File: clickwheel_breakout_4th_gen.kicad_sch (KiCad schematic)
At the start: 7 parts

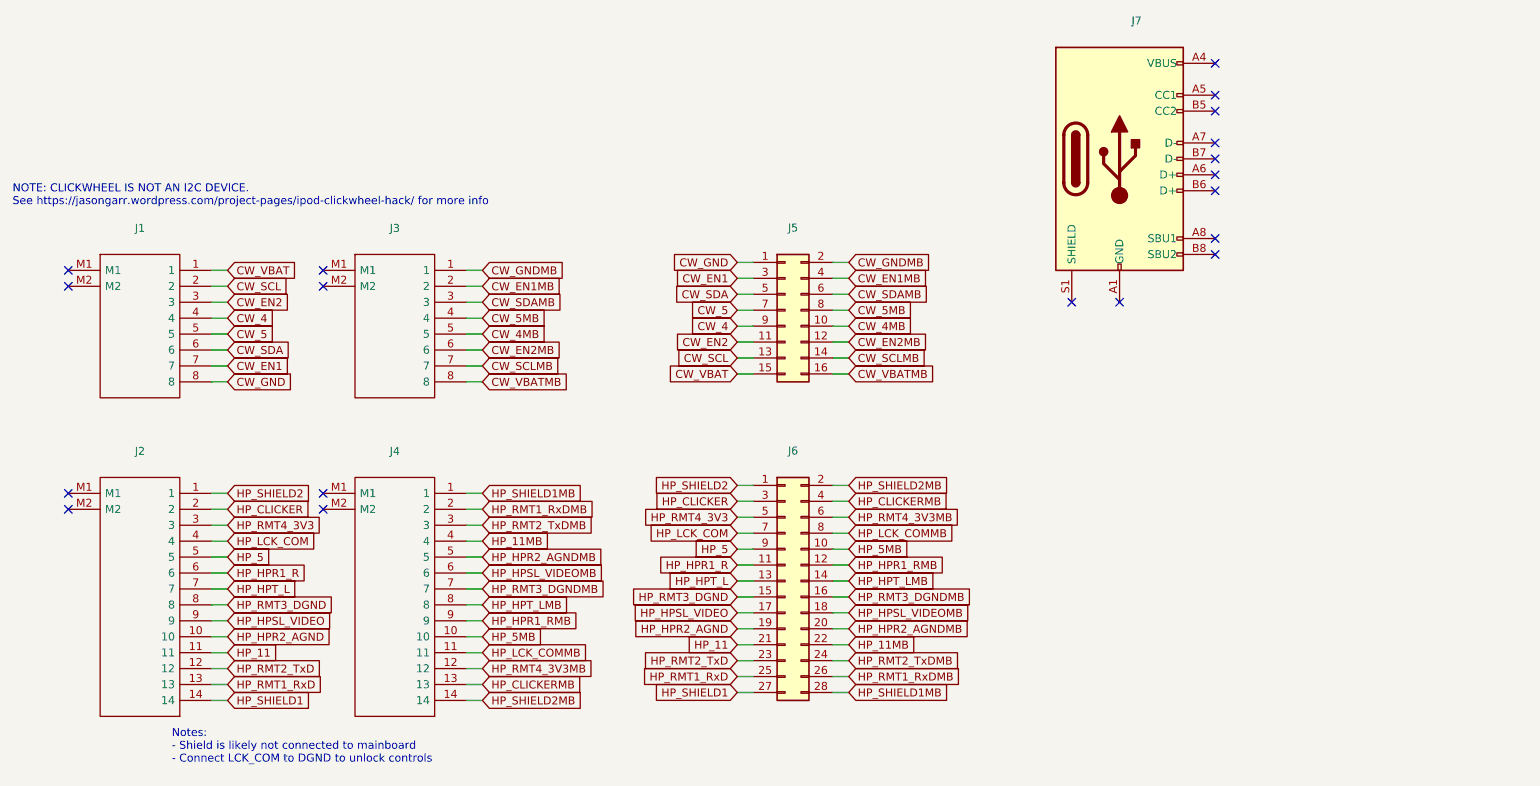
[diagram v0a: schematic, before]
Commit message: kibot: add initial generated QR code
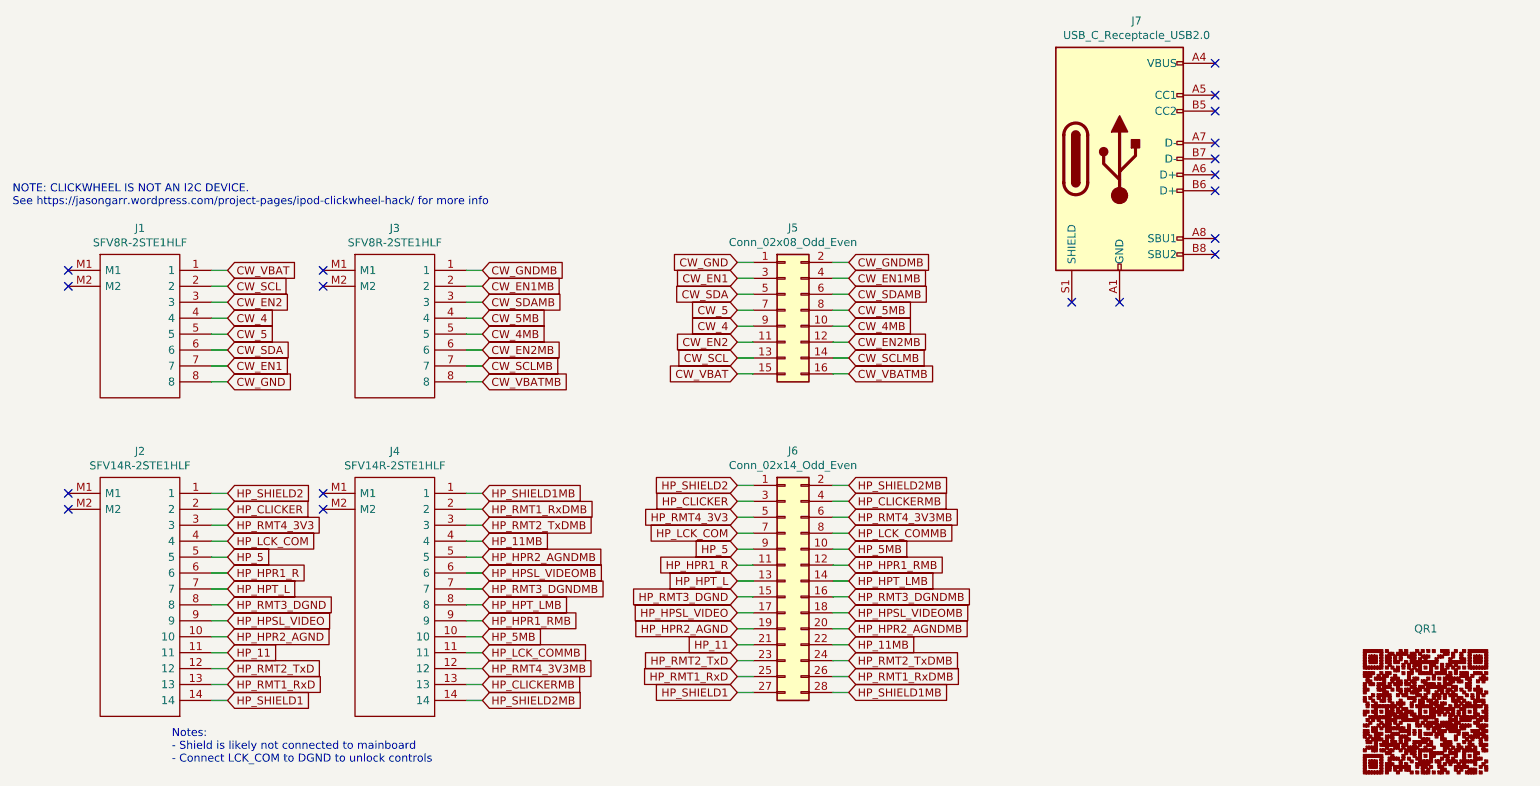
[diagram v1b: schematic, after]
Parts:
- added QR1: (no value), QR:QR_data, symbol clickwheel_breakout_4th_gen-qr:QR_data
- J1, J3: value (none) -> SFV8R-2STE1HLF; footprint (none) -> Gigahawk:SFV8R2STE1HLF
- J2, J4: value (none) -> SFV14R-2STE1HLF; footprint (none) -> Gigahawk:SFV14R2STE1HLF
- J5: value (none) -> Conn_02x08_Odd_Even; footprint (none) -> Connector_PinHeader_2.54mm:PinHeader_2x08_P2.54mm_Vertical
- J6: value (none) -> Conn_02x14_Odd_Even; footprint (none) -> Connector_PinHeader_2.54mm:PinHeader_2x14_P2.54mm_Vertical
- J7: value (none) -> USB_C_Receptacle_USB2.0; footprint (none) -> Gigahawk:USB_C_Receptacle_GCT_USB4085
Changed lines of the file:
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@@
     (in_bom yes) (on_board yes)
     (property "Reference" "J2" (id 0) (at 49.53 106.299 0))
-    (property "Value" "" (id 1) (at 49.53 108.6104 0))
-    (property "Footprint" "" (id 2) (at 57.15 110.49 0)
+    (property "Value" "SFV14R-2STE1HLF" (id 1) (at 49.53 108.6104 0))
+    (property "Footprint" "Gigahawk:SFV14R2STE1HLF" (id 2) (at 57.15 110.49 0)
       (effects (font (size 1.27 1.27)) (justify left) hide)
     )
@@
     (in_bom yes) (on_board yes)
     (property "Reference" "J1" (id 0) (at 49.53 70.739 0))
-    (property "Value" "" (id 1) (at 49.53 73.0504 0))
-    (property "Footprint" "" (id 2) (at 57.15 74.93 0)
+    (property "Value" "SFV8R-2STE1HLF" (id 1) (at 49.53 73.0504 0))
+    (property "Footprint" "Gigahawk:SFV8R2STE1HLF" (id 2) (at 57.15 74.93 0)
       (effects (font (size 1.27 1.27)) (justify left) hide)
     )
@@
     (in_bom yes) (on_board yes)
     (property "Reference" "J4" (id 0) (at 90.17 106.299 0))
-    (property "Value" "" (id 1) (at 90.17 108.6104 0))
-    (property "Footprint" "" (id 2) (at 97.79 110.49 0)
+    (property "Value" "SFV14R-2STE1HLF" (id 1) (at 90.17 108.6104 0))
+    (property "Footprint" "Gigahawk:SFV14R2STE1HLF" (id 2) (at 97.79 110.49 0)
       (effects (font (size 1.27 1.27)) (justify left) hide)
     )
@@
     (in_bom yes) (on_board yes)
     (property "Reference" "J3" (id 0) (at 90.17 70.739 0))
-    (property "Value" "" (id 1) (at 90.17 73.0504 0))
-    (property "Footprint" "" (id 2) (at 97.79 74.93 0)
+    (property "Value" "SFV8R-2STE1HLF" (id 1) (at 90.17 73.0504 0))
+    (property "Footprint" "Gigahawk:SFV8R2STE1HLF" (id 2) (at 97.79 74.93 0)
       (effects (font (size 1.27 1.27)) (justify left) hide)
     )
@@
     (in_bom yes) (on_board yes)
     (property "Reference" "J5" (id 0) (at 153.67 70.6882 0))
-    (property "Value" "" (id 1) (at 153.67 72.9996 0))
-    (property "Footprint" "" (id 2) (at 152.4 83.82 0)
+    (property "Value" "Conn_02x08_Odd_Even" (id 1) (at 153.67 72.9996 0))
+    (property "Footprint" "Connector_PinHeader_2.54mm:PinHeader_2x08_P2.54mm_Vertical" (id 2) (at 152.4 83.82 0)
       (effects (font (size 1.27 1.27)) hide)
     )
@@
     (in_bom yes) (on_board yes)
     (property "Reference" "J6" (id 0) (at 153.67 106.2482 0))
-    (property "Value" "" (id 1) (at 153.67 108.5596 0))
-    (property "Footprint" "" (id 2) (at 152.4 127 0)
+    (property "Value" "Conn_02x14_Odd_Even" (id 1) (at 153.67 108.5596 0))
+    (property "Footprint" "Connector_PinHeader_2.54mm:PinHeader_2x14_P2.54mm_Vertical" (id 2) (at 152.4 127 0)
       (effects (font (size 1.27 1.27)) hide)
     )
@@
     (in_bom yes) (on_board yes)
     (property "Reference" "J7" (id 0) (at 208.4578 37.6682 0))
-    (property "Value" "" (id 1) (at 208.4578 39.9796 0))
-    (property "Footprint" "" (id 2) (at 209.55 59.69 0)
+    (property "Value" "USB_C_Receptacle_USB2.0" (id 1) (at 208.4578 39.9796 0))
+    (property "Footprint" "Gigahawk:USB_C_Receptacle_GCT_USB4085" (id 2) (at 209.55 59.69 0)
       (effects (font (size 1.27 1.27)) hide)
     )
@@
     (pin "S1")
   )
+  (symbol (lib_id "clickwheel_breakout_4th_gen-qr:QR_data") (at 254.635 147.955 0) (unit 1)
+    (in_bom no) (on_board yes)
+    (property "Reference" "QR1" (id 0) (at 252.73 134.62 0)
+      (effects (font (size 1.27 1.27)) (justify left))
+    )
+    (property "Value" "" (id 1) (at 250.825 136.525 0)
+      (effects (font (size 1.27 1.27)) (justify left))
+    )
+    (property "Footprint" "QR:QR_data" (id 2) (at 254.635 158.405 0)
+      (effects (font (size 1.27 1.27)) hide)
+    )
+    (property "Datasheet" "" (id 3) (at 254.635 160.105 0)
+      (effects (font (size 1.27 1.27)) hide)
+    )
+    (property "qr_version" "7" (id 4) (at 254.635 161.805 0)
+      (effects (font (size 1.27 1.27)) hide)
+    )
+    (property "qr_size" "45" (id 5) (at 254.635 163.505 0)
+      (effects (font (size 1.27 1.27)) hide)
+    )
+    (property "qr_ecc" "0,1" (id 6) (at 254.635 165.205 0)
+      (effects (font (size 1.27 1.27)) hide)
+    )
+    (property "qr_mask" "3" (id 7) (at 254.635 166.905 0)
+      (effects (font (size 1.27 1.27)) hide)
+    )
+    (property "qr_text" "OOPSIE WOOPSIE!! Uwu We make a fucky wucky!! A wittle fucko boingo! The code monkeys at our headquarters are working VEWY HAWD to fix this!\n" (id 8) (at 254.635 168.605 0)
+      (effects (font (size 1.27 1.27)) hide)
+    )
+  )
   (sheet_instances
     (path "/" (page "1"))
@@
       (reference "J7") (unit 1) (value "USB_C_Receptacle_USB2.0") (footprint "Gigahawk:USB_C_Receptacle_GCT_USB4085")
     )
-  )
+    (path "/90211c05-3354-414f-a4b4-596a1a6ea313"
+      (reference "QR1") (unit 1) (value "QR_data") (footprint "QR:QR_data")
+    )
+  )

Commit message: ci: add CI (#1)
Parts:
- removed QR1: (no value), QR:QR_data, symbol clickwheel_breakout_4th_gen-qr:QR_data
- added QR1: (no value), symbol QR:QR_data
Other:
- title: (none) -> iPod 4th Gen Clickwheel Breakout
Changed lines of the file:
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@@
 (kicad_sch (version 20211123) (generator eeschema)
   (paper "A4")
+  (title_block
+    (title "iPod 4th Gen Clickwheel Breakout")
+    (date "${DATE}")
+    (rev "${REVISION}")
+  )
   (no_connect (at 78.74 77.47))
   (no_connect (at 78.74 80.01))
@@
     (pin "S1")
   )
-  (symbol (lib_id "clickwheel_breakout_4th_gen-qr:QR_data") (at 254.635 147.955 0) (unit 1)
-    (in_bom no) (on_board yes)
-    (property "Reference" "QR1" (id 0) (at 252.73 134.62 0)
-      (effects (font (size 1.27 1.27)) (justify left))
-    )
-    (property "Value" "" (id 1) (at 250.825 136.525 0)
-      (effects (font (size 1.27 1.27)) (justify left))
-    )
-    (property "Footprint" "QR:QR_data" (id 2) (at 254.635 158.405 0)
-      (effects (font (size 1.27 1.27)) hide)
-    )
-    (property "Datasheet" "" (id 3) (at 254.635 160.105 0)
-      (effects (font (size 1.27 1.27)) hide)
-    )
-    (property "qr_version" "7" (id 4) (at 254.635 161.805 0)
-      (effects (font (size 1.27 1.27)) hide)
-    )
-    (property "qr_size" "45" (id 5) (at 254.635 163.505 0)
-      (effects (font (size 1.27 1.27)) hide)
-    )
-    (property "qr_ecc" "0,1" (id 6) (at 254.635 165.205 0)
-      (effects (font (size 1.27 1.27)) hide)
-    )
-    (property "qr_mask" "3" (id 7) (at 254.635 166.905 0)
-      (effects (font (size 1.27 1.27)) hide)
-    )
-    (property "qr_text" "OOPSIE WOOPSIE!! Uwu We make a fucky wucky!! A wittle fucko boingo! The code monkeys at our headquarters are working VEWY HAWD to fix this!\n" (id 8) (at 254.635 168.605 0)
+  (symbol (lib_id "QR:QR_data") (at 260.985 145.415 0) (unit 1)
+    (in_bom no) (on_board yes) (fields_autoplaced)
+    (property "Reference" "QR1" (id 0) (at 260.885 130.81 0))
+    (property "Value" "" (id 1) (at 260.885 133.35 0))
+    (property "Footprint" "" (id 2) (at 260.985 158.365 0)
+      (effects (font (size 1.27 1.27)) hide)
+    )
+    (property "Datasheet" "" (id 3) (at 260.985 160.065 0)
+      (effects (font (size 1.27 1.27)) hide)
+    )
+    (property "qr_version" "7" (id 4) (at 260.985 161.765 0)
+      (effects (font (size 1.27 1.27)) hide)
+    )
+    (property "qr_size" "45" (id 5) (at 260.985 163.465 0)
+      (effects (font (size 1.27 1.27)) hide)
+    )
+    (property "qr_ecc" "0,1" (id 6) (at 260.985 165.165 0)
+      (effects (font (size 1.27 1.27)) hide)
+    )
+    (property "qr_mask" "3" (id 7) (at 260.985 166.865 0)
+      (effects (font (size 1.27 1.27)) hide)
+    )
+    (property "qr_text" "OOPSIE WOOPSIE!! Uwu We make a fucky wucky!! A wittle fucko boingo! The code monkeys at our headquarters are working VEWY HAWD to fix this!\n" (id 8) (at 260.985 168.565 0)
       (effects (font (size 1.27 1.27)) hide)
     )
@@
       (reference "J7") (unit 1) (value "USB_C_Receptacle_USB2.0") (footprint "Gigahawk:USB_C_Receptacle_GCT_USB4085")
     )
-    (path "/90211c05-3354-414f-a4b4-596a1a6ea313"
+    (path "/e1d122d3-e0b7-44f3-b2d8-4baa56b4ef17"
       (reference "QR1") (unit 1) (value "QR_data") (footprint "QR:QR_data")
     )

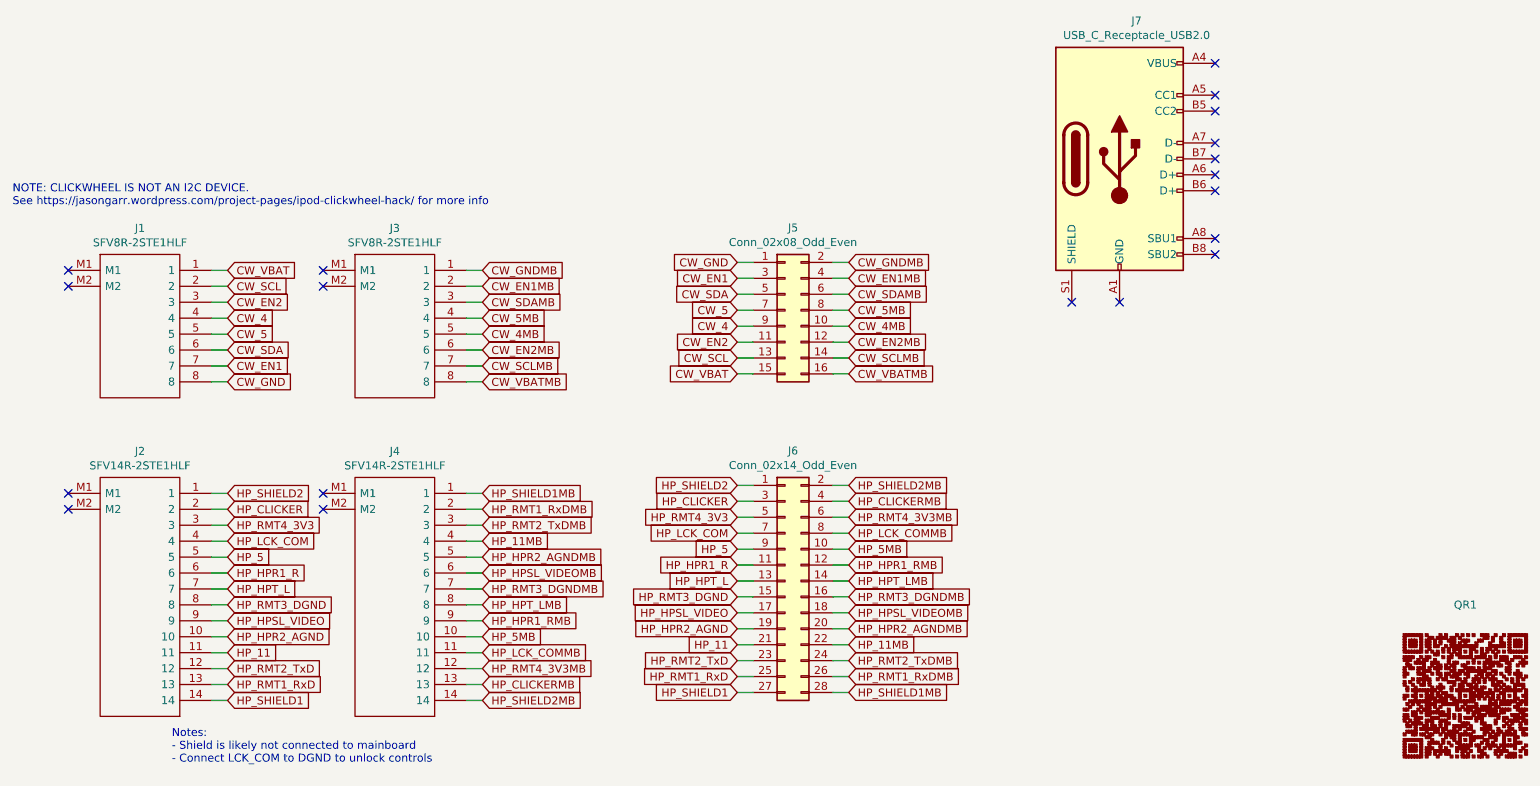
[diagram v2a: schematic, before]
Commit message: silkscreen: add label for missing headphone AGND
- silkscreen: add connection instructions
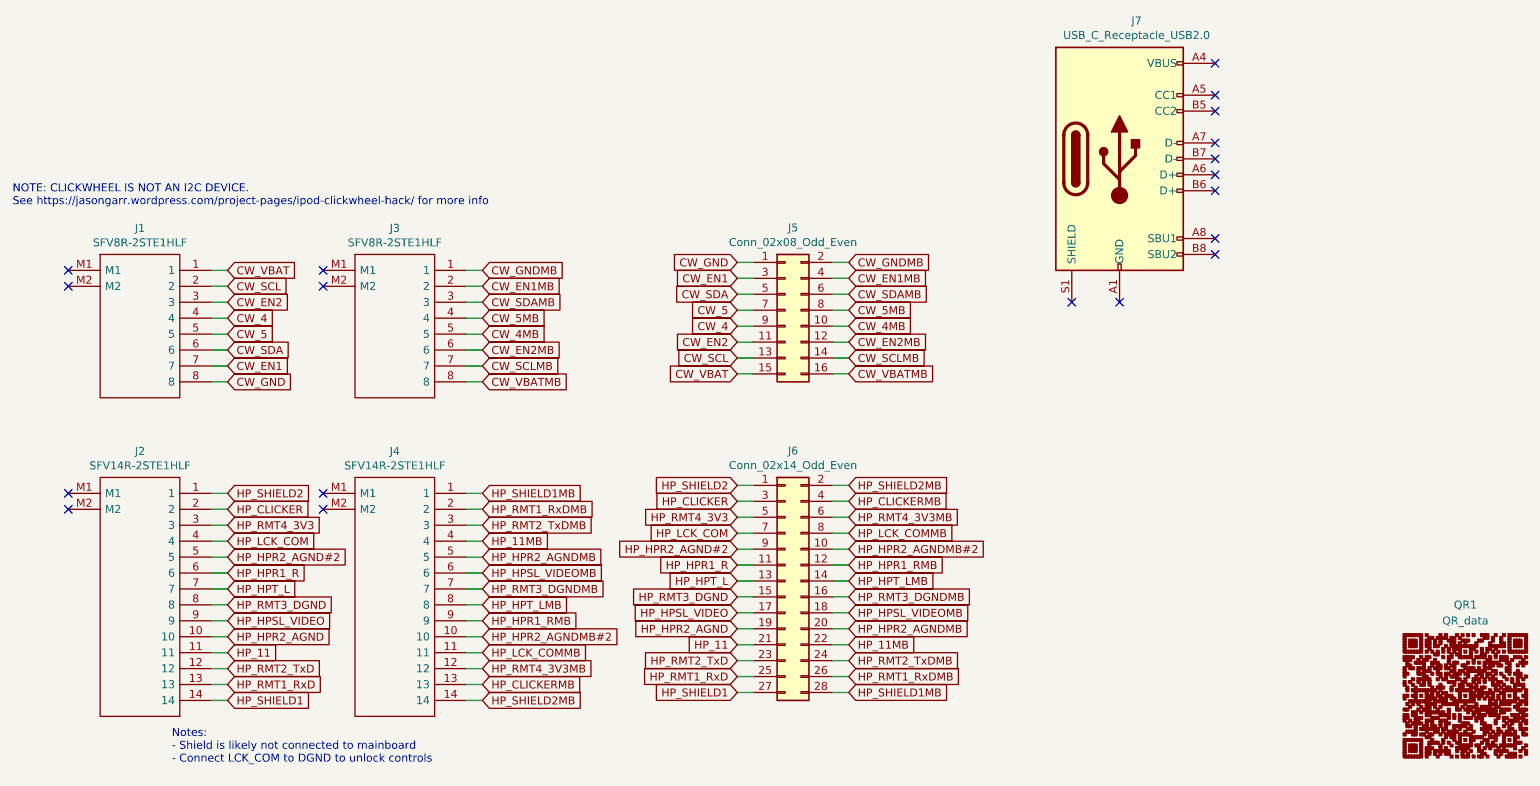
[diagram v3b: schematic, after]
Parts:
- QR1: value (none) -> QR_data; footprint (none) -> QR:QR_data
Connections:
- net HP_5 renamed HP_HPR2_AGND#2
- net HP_5MB renamed HP_HPR2_AGNDMB#2
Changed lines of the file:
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@@
+    )
+  )
+  (global_label "HP_HPR2_AGNDMB#2" (shape input) (at 162.56 121.92 0) (fields_autoplaced)
+    (effects (font (size 1.27 1.27)) (justify left))
+    (property "Intersheet References" "${INTERSHEET_REFS}" (id 0) (at 184.6599 121.8406 0)
+      (effects (font (size 1.27 1.27)) (justify left) hide)
     )
   )
@@
     )
   )
-  (global_label "HP_5MB" (shape input) (at 104.14 135.89 0) (fields_autoplaced)
-    (effects (font (size 1.27 1.27)) (justify left))
-    (property "Intersheet References" "${INTERSHEET_REFS}" (id 0) (at 0 0 0)
-      (effects (font (size 1.27 1.27)) hide)
-    )
-  )
   (global_label "HP_RMT2_TxD" (shape input) (at 63.5 140.97 0) (fields_autoplaced)
     (effects (font (size 1.27 1.27)) (justify left))
@@
     )
   )
+  (global_label "HP_HPR2_AGND#2" (shape input) (at 63.5 123.19 0) (fields_autoplaced)
+    (effects (font (size 1.27 1.27)) (justify left))
+    (property "Intersheet References" "${INTERSHEET_REFS}" (id 0) (at 82.8785 123.1106 0)
+      (effects (font (size 1.27 1.27)) (justify left) hide)
+    )
+  )
   (global_label "CW_GNDMB" (shape input) (at 162.56 76.2 0) (fields_autoplaced)
     (effects (font (size 1.27 1.27)) (justify left))
@@
     )
   )
-  (global_label "HP_5MB" (shape input) (at 162.56 121.92 0) (fields_autoplaced)
-    (effects (font (size 1.27 1.27)) (justify left))
-    (property "Intersheet References" "${INTERSHEET_REFS}" (id 0) (at 0 0 0)
-      (effects (font (size 1.27 1.27)) hide)
-    )
-  )
   (global_label "HP_CLICKER" (shape input) (at 144.78 114.3 180) (fields_autoplaced)
     (effects (font (size 1.27 1.27)) (justify right))
@@
     )
   )
-  (global_label "HP_5" (shape input) (at 144.78 121.92 180) (fields_autoplaced)
-    (effects (font (size 1.27 1.27)) (justify right))
-    (property "Intersheet References" "${INTERSHEET_REFS}" (id 0) (at 0 0 0)
-      (effects (font (size 1.27 1.27)) hide)
-    )
-  )
   (global_label "HP_RMT1_RxD" (shape input) (at 144.78 142.24 180) (fields_autoplaced)
     (effects (font (size 1.27 1.27)) (justify right))
@@
     )
   )
+  (global_label "HP_HPR2_AGND#2" (shape input) (at 144.78 121.92 180) (fields_autoplaced)
+    (effects (font (size 1.27 1.27)) (justify right))
+    (property "Intersheet References" "${INTERSHEET_REFS}" (id 0) (at 125.4015 121.9994 0)
+      (effects (font (size 1.27 1.27)) (justify right) hide)
+    )
+  )
   (global_label "CW_EN2MB" (shape input) (at 104.14 90.17 0) (fields_autoplaced)
     (effects (font (size 1.27 1.27)) (justify left))
@@
     )
   )
+  (global_label "HP_HPR2_AGNDMB#2" (shape input) (at 104.14 135.89 0) (fields_autoplaced)
+    (effects (font (size 1.27 1.27)) (justify left))
+    (property "Intersheet References" "${INTERSHEET_REFS}" (id 0) (at 126.2399 135.8106 0)
+      (effects (font (size 1.27 1.27)) (justify left) hide)
+    )
+  )
   (global_label "HP_HPT_LMB" (shape input) (at 104.14 130.81 0) (fields_autoplaced)
     (effects (font (size 1.27 1.27)) (justify left))
@@
   )
   (global_label "HP_SHIELD2MB" (shape input) (at 104.14 146.05 0) (fields_autoplaced)
-    (effects (font (size 1.27 1.27)) (justify left))
-    (property "Intersheet References" "${INTERSHEET_REFS}" (id 0) (at 0 0 0)
-      (effects (font (size 1.27 1.27)) hide)
-    )
-  )
-  (global_label "HP_5" (shape input) (at 63.5 123.19 0) (fields_autoplaced)
     (effects (font (size 1.27 1.27)) (justify left))
     (property "Intersheet References" "${INTERSHEET_REFS}" (id 0) (at 0 0 0)
@@
     (in_bom no) (on_board yes) (fields_autoplaced)
     (property "Reference" "QR1" (id 0) (at 260.885 130.81 0))
-    (property "Value" "" (id 1) (at 260.885 133.35 0))
-    (property "Footprint" "" (id 2) (at 260.985 158.365 0)
-      (effects (font (size 1.27 1.27)) hide)
-    )
+    (property "Value" "QR_data" (id 1) (at 260.885 133.35 0))
+    (property "Footprint" "QR:QR_data" (id 2) (at 260.985 158.365 0)
+      (effects (font (size 1.27 1.27)) hide)
+    )
